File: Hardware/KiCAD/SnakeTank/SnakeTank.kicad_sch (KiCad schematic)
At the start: 4 parts, among them J1 USB4105-GF-A, U1 ESP32-S3

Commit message: Lots of hardware updates
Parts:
- removed J1: USB4105-GF-A, USB4105-GF-A:GCT_USB4105-GF-A, symbol USB4105-GF-A:USB4105-GF-A
- removed U1: ESP32-S3, Package_DFN_QFN:QFN-56-1EP_7x7mm_P0.4mm_EP4x4mm, symbol MCU_Espressif:ESP32-S3
- added BOOT1, RESET1: ~, Button_Switch_SMD:SW_SPST_PTS810, symbol Switch:SW_MEC_5E
- added C1, C11, C2, C3, C6: 10uF, Capacitor_SMD:C_0603_1608Metric, symbol Device:C_Small
- added C10, C4, C5: 0.1uF, Capacitor_SMD:C_0603_1608Metric, symbol Device:C_Small
- added C12: 1uF, Capacitor_SMD:C_0603_1608Metric, symbol Device:C_Small
- added C7: 100nF, Capacitor_SMD:C_0603_1608Metric, symbol Device:C_Small
- added C8, C9: 47pF, Capacitor_SMD:C_0603_1608Metric, symbol Device:C_Small
- added D3: LED, LED_SMD:LED_0603_1608Metric, symbol Device:LED
- added J2: USB_C_Receptacle_USB2.0_16P, symbol Connector:USB_C_Receptacle_USB2.0_16P
- added Q1, Q2: L8050QLT1G, SOT-23_LRC, symbol 2024-08-29_22-52-09:L8050QLT1G
- added R10, R11: 0, symbol Device:R_Small
- added R3, R8, R9: 10K, symbol Device:R_Small
- added R4, R6: 47, symbol Device:R_Small
- added R5: 1k, Resistor_SMD:R_0603_1608Metric, symbol Device:R_Small
- added R7: 0, Resistor_SMD:R_0603_1608Metric, symbol Device:R_Small
- added U1: LP2985-3.3, Package_TO_SOT_SMD:SOT-23-5, symbol Regulator_Linear:LP2985-3.3
- added U2: ESP32-S3-WROOM-1-N8, ESP32-S3-WROOM-1-N8:XCVR_ESP32-S3-WROOM-1-N8, symbol ESP32-S3-WROOM-1-N8:ESP32-S3-WROOM-1-N8
- added U3: ESD7104MUTAG, Package_DFN_QFN:Diodes_UDFN-10_1.0x2.5mm_P0.5mm, symbol Power_Protection:D3V3XA4B10LP
- added U4: FT231XS, Package_SO:SSOP-20_3.9x8.7mm_P0.635mm, symbol Interface_USB:FT231XS
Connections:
- net GND: now also R2.2, BOOT1.1, BOOT1.2, C1.2, C10.2, C11.2, C12.2, C2.2, C3.2, C4.2, C5.2, C6.2, C7.2, C8.2, C9.2, D3.1 (K), J2.A1 (GND), J2.A12 (GND), J2.B1 (GND), J2.B12 (GND), J2.S1 (SHIELD), RESET1.1, RESET1.2, U1.2 (GND), U2.1 (GND), U2.40 (GND), U2.41_1 (GND), U2.41_2 (GND), U2.41_3 (GND), U2.41_4 (GND), U2.41_5 (GND), U2.41_6 (GND), U2.41_7 (GND), U2.41_8 (GND), U2.41_9 (GND), U3.3 (VSS), U3.8 (VSS), U4.16 (GND), U4.6 (GND); no longer R2.1
- net at R1.1: now also J2.B5 (CC2)
- new net: C3.1, U1.4 (BP)
- new net: Q2.1, R9.2
- new net: Q2.3, R11.1
- new net: D3.2 (A), R5.2
- new net: R4.2, U4.12 (USBDM)
- new net: Q1.1, R8.2
- new net: Q1.3, R10.1
- new net: R6.1, U4.11 (USBDP)
- new net: J2.A5 (CC1), R2.1
- new net: C7.1, U4.13 (3V3OUT), U4.14 (~{RESET}), U4.3 (VCCIO)
- new net +3.3V: C10.1, C11.1, C2.1, R5.1, R7.2, U1.5 (VOUT)
- new net +5V: C1.1, C6.1, J2.A4 (VBUS), J2.A9 (VBUS), J2.B4 (VBUS), J2.B9 (VBUS), U1.1 (VIN), U1.3 (ON/~{OFF}), U3.4, U3.7 (NC), U4.15 (VCC)
- new net CHIP_PU: C12.1, C4.1, R10.2, R3.2, RESET1.3 (K), RESET1.4 (A)
- new net DHT11_1_data: U2.4 (IO4)
- new net DHT11_2_data: U2.6 (IO6)
- new net ESP_3V3: R3.1, R7.1, U2.2 (3V3)
- new net FDTI_UART_TX: U4.20 (TXD)
- new net FTDI_DTR: Q1.2, R9.1, U4.1 (~{DTR})
- new net FTDI_RTS: Q2.2, R8.1, U4.2 (~{RTS})
- new net FTDI_UART_RX: U4.4 (RXD)
- new net GPIO_0: BOOT1.3 (K), BOOT1.4 (A), C5.1, R11.2, U2.27 (IO0)
- new net LCD_D4: U2.31 (IO38)
- new net LCD_D5: U2.32 (IO39)
- new net LCD_D6: U2.33 (IO40)
- new net LCD_D7: U2.34 (IO41)
- new net LCD_E: U2.28 (IO35)
- new net LCD_RW: U2.26 (IO45)
- new net UART_RX: U2.37 (TXD0)
- new net UART_TX: U2.36 (RXD0)
- new net USB_N: C9.1, J2.A6 (D+), J2.B6 (D+), R4.1, U3.1, U3.10 (NC)
- new net USB_P: C8.1, J2.A7 (D-), J2.B7 (D-), R6.2, U3.2, U3.9 (NC)
- no-connect marks 2 -> 10
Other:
- added sheet Untitled Sheet (untitled.kicad_sch)
- note added: "Datasheet:https://ftdichip.com/wp-content/uploads/2024/05/DS_FT231X.pdf Says to use Ferrite bead for VCC input"
- note added: "Keeping these NC for simplicity"
- title: (none) -> SnakeTank
- moved on the sheet: R1, R2

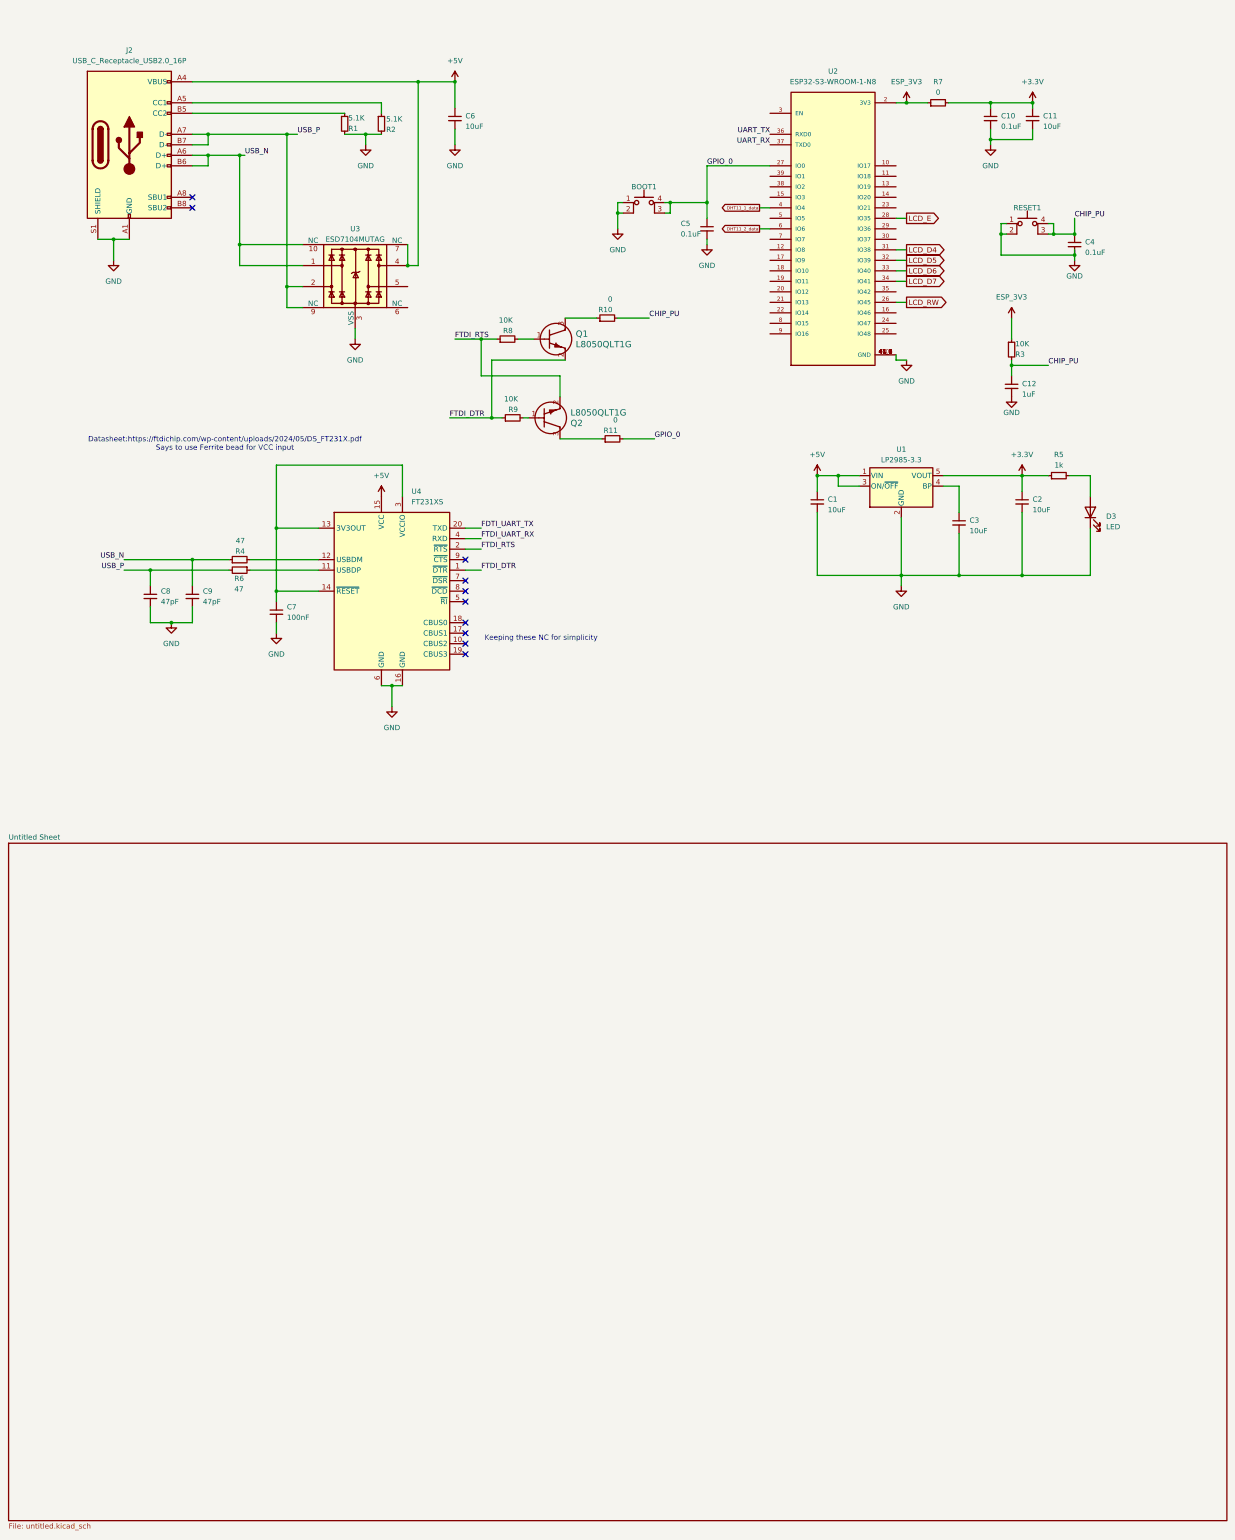
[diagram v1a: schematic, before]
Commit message: Updated schematic and export PDF
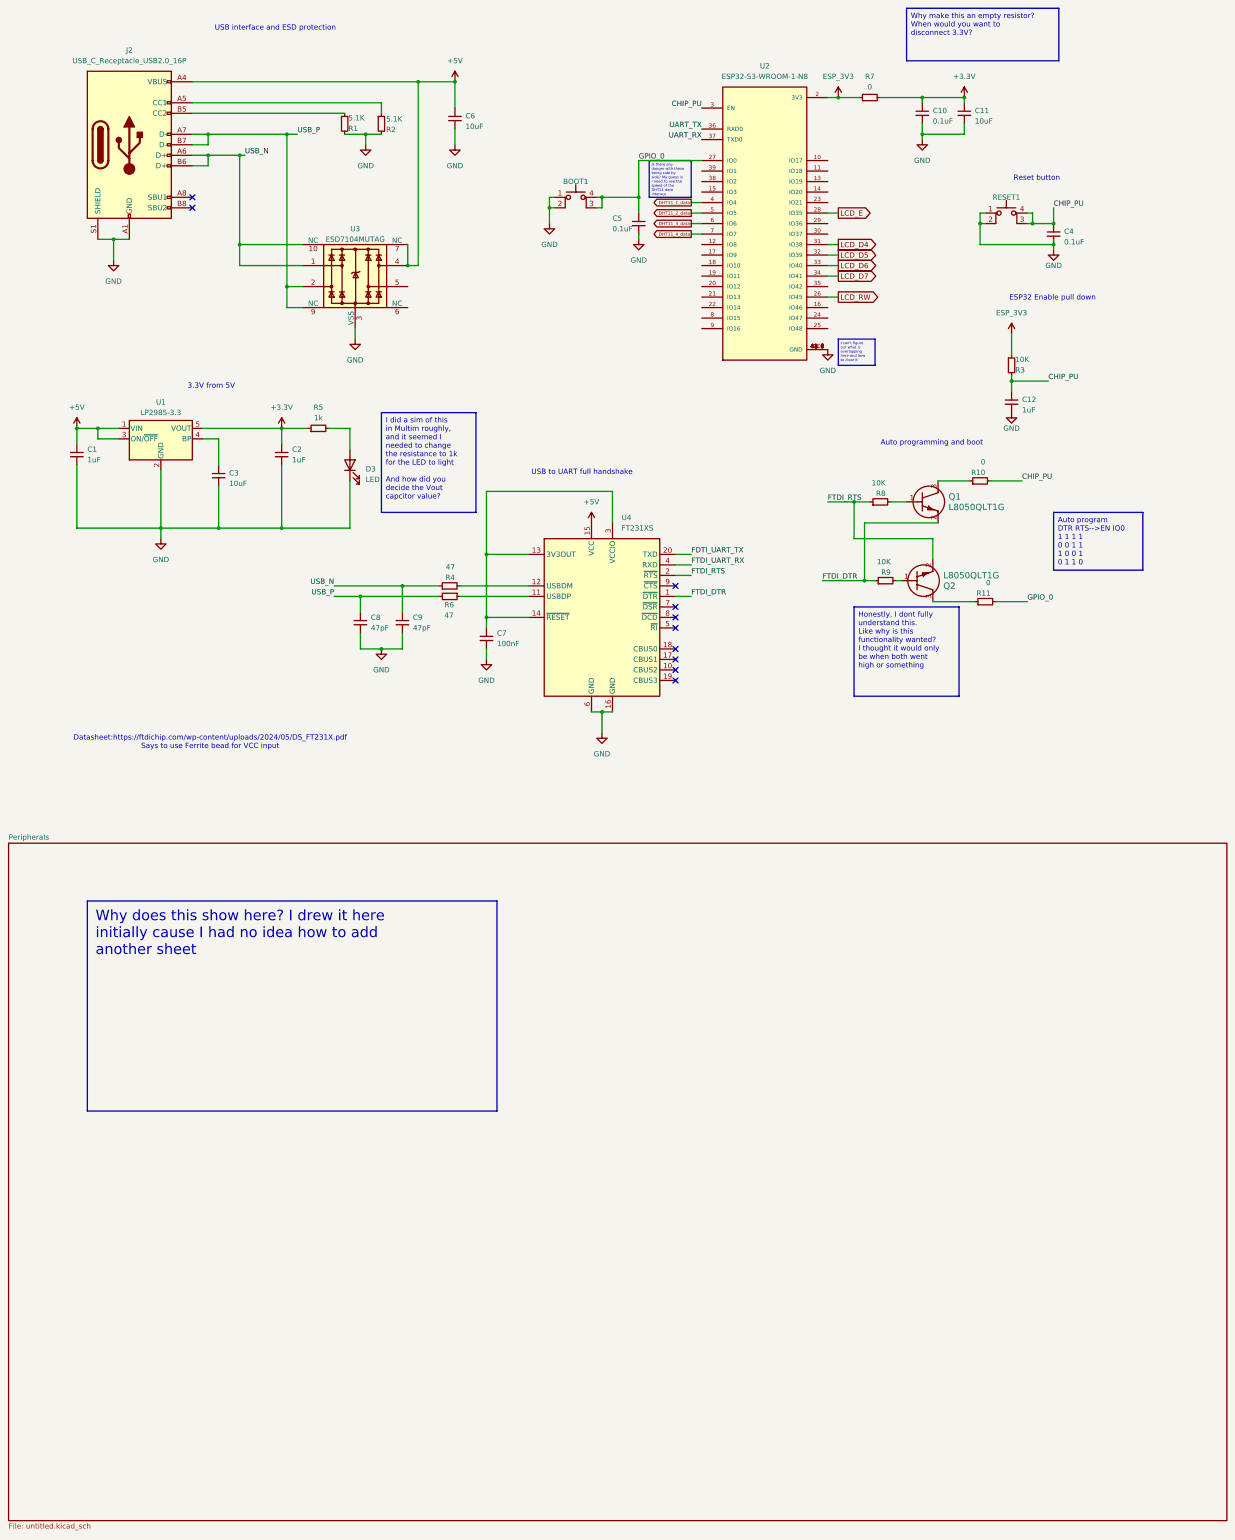
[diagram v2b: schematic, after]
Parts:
- C1, C2: value 10uF -> 1uF
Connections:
- net CHIP_PU: now also U2.3 (EN)
- net DHT11_2_data: now also U2.5 (IO5); no longer U2.6 (IO6)
- net DHT11_4_data: now reaches U2.7 (IO7)
- new net DHT11_3_data: U2.6 (IO6)
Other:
- sheet Untitled Sheet renamed Peripherals
- note added: "3.3V from 5V"
- note added: "Auto programming and boot"
- note added: "ESP32 Enable pull down"
- note added: "Reset button"
- note added: "USB interface and ESD protection"
- note added: "USB to UART full handshake"
- note removed: "Keeping these NC for simplicity"
- moved on the sheet: BOOT1, C1, C10, C11, C12, C2, C3, C4, C5, C7, C8, C9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

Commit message: hardware work
finishing schematic and footprints
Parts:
- removed U3: ESD7104MUTAG, Package_DFN_QFN:Diodes_UDFN-10_1.0x2.5mm_P0.5mm, symbol Power_Protection:D3V3XA4B10LP
- added D1, D2: ESD321DPYR, ESD321DPYR:TVS_ESD321DPYR, symbol ESD321DPYR:ESD321DPYR
- added FB1: FerriteBead, FerriteBead:BEADC0603X33N, symbol Device:FerriteBead
- C6: value 10uF -> 10nF
- J2: footprint (none) -> Connector_USB:USB_C_Receptacle_JAE_DX07S016JA1R1500
- Q1, Q2: footprint SOT-23_LRC -> Package_TO_SOT_SMD:SOT-23-3
- R1, R10, R11, R2, R3, R4, R6, R8, R9: footprint (none) -> Resistor_SMD:R_0603_1608Metric
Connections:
- net UART_RX is gone; now on net FTDI_UART_RX: U2.37 (TXD0)
- net UART_TX is gone; now on net FDTI_UART_TX: U2.36 (RXD0)
- net +5V: now also FB1.1; no longer J2.A4 (VBUS), J2.A9 (VBUS), J2.B4 (VBUS), J2.B9 (VBUS)
- net GND: now also D1.2, D2.2
- net USB_N: now also J2.A7 (D-), J2.B7 (D-), D2.1; no longer J2.A6 (D+), J2.B6 (D+)
- net USB_P: now also J2.A6 (D+), J2.B6 (D+), D1.1; no longer J2.A7 (D-), J2.B7 (D-)
- net IO17: now reaches U2.10 (IO17)
- net IO18: now reaches U2.11 (IO18)
- net IO8: now reaches U2.12 (IO8)
- net IO19: now reaches U2.13 (IO19)
- net IO20: now reaches U2.14 (IO20)
- net IO3: now reaches U2.15 (IO3)
- net IO46: now reaches U2.16 (IO46)
- net IO9: now reaches U2.17 (IO9)
- net IO10: now reaches U2.18 (IO10)
- net IO11: now reaches U2.19 (IO11)
- net IO12: now reaches U2.20 (IO12)
- net IO13: now reaches U2.21 (IO13)
- net IO14: now reaches U2.22 (IO14)
- net IO21: now reaches U2.23 (IO21)
- net IO47: now reaches U2.24 (IO47)
- net IO48: now reaches U2.25 (IO48)
- net IO36: now reaches U2.29 (IO36)
- net IO37: now reaches U2.30 (IO37)
- net IO42: now reaches U2.35 (IO42)
- net IO2: now reaches U2.38 (IO2)
- net IO1: now reaches U2.39 (IO1)
- net IO15: now reaches U2.8 (IO15)
- net IO16: now reaches U2.9 (IO16)
- net LCD_RW renamed LCD_RS
- new net: FB1.2, J2.A4 (VBUS), J2.A9 (VBUS), J2.B4 (VBUS), J2.B9 (VBUS)
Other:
- sheet Peripherals: file untitled.kicad_sch -> Peripherals.kicad_sch
- note added: "Datasheet:https://ftdichip.com/wp-content/uploads/2024/05/DS_FT231X.pdf"
- note added: "USB interface, Power, and ESD protection"
- note removed: "Datasheet:https://ftdichip.com/wp-content/uploads/2024/05/DS_FT231X.pdf Says to use Ferrite bead for VCC input"
- note removed: "USB interface and ESD protection"
- moved on the sheet: BOOT1, C10, C11, C12, C4, C5, R10, R11, R3, R7, RESET1, U2

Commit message: layout Rough
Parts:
- added R12, R13, R14, R15: 5K, Resistor_SMD:R_0603_1608Metric, symbol Device:R_Small
- added R16: 0, Resistor_SMD:R_0603_1608Metric, symbol Device:R_Small
- added TP1: CHIP_PU_TP, TestPoint:TestPoint_Pad_D1.5mm, symbol Connector:TestPoint
- added TP2: 3V3_TP, TestPoint:TestPoint_Pad_D1.5mm, symbol Connector:TestPoint
- added TP3: USB_5V_TP, TestPoint:TestPoint_Pad_D1.5mm, symbol Connector:TestPoint
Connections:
- net IO15 is gone; now on net LCD_RS: U2.8 (IO15)
- net IO16 is gone; now on net LCD_E: U2.9 (IO16)
- net IO17 is gone; now on net LCD_D4: U2.10 (IO17)
- net IO18 is gone; now on net LCD_D5: U2.11 (IO18)
- net IO19 is gone; now on net LCD_D6: U2.13 (IO19)
- net IO20 is gone; now on net LCD_D7: U2.14 (IO20)
- net +3.3V: now also TP2.1
- net +5V: now also R12.1, R13.1, R14.1, R15.1, TP3.1
- net CHIP_PU: now also TP1.1
- net DHT11_1_data: now also R15.2
- net DHT11_2_data: now also R14.2
- net DHT11_3_data: now also R13.2
- net DHT11_4_data: now also R12.2
- net FTDI_DTR: now also R16.1; no longer Q1.2, R9.1
- net LCD_D4: no longer U2.31 (IO38)
- net LCD_D5: no longer U2.32 (IO39)
- net LCD_D6: no longer U2.33 (IO40)
- net LCD_D7: no longer U2.34 (IO41)
- net LCD_E: no longer U2.28 (IO35)
- net LCD_RS: no longer U2.26 (IO45)
- net USBN: now reaches R4.2, U4.12 (USBDM)
- net USBP: now reaches R6.1, U4.11 (USBDP)
- net IO1: no longer names the net of U2.39 (IO1)
- net IO2: no longer names the net of U2.38 (IO2)
- net IO36: no longer names the net of U2.29 (IO36)
- net IO37: no longer names the net of U2.30 (IO37)
- net IO42: no longer names the net of U2.35 (IO42)
- new net: Q1.2, R16.2, R9.1
- new net IO45: U2.26 (IO45)
- no-connect marks 10 -> 20
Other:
- moved on the sheet: BOOT1, C12, C4, C5, R3, RESET1
